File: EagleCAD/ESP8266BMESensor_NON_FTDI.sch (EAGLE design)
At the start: 21 parts, among them J1 AMP FCI 10103594-0001LF

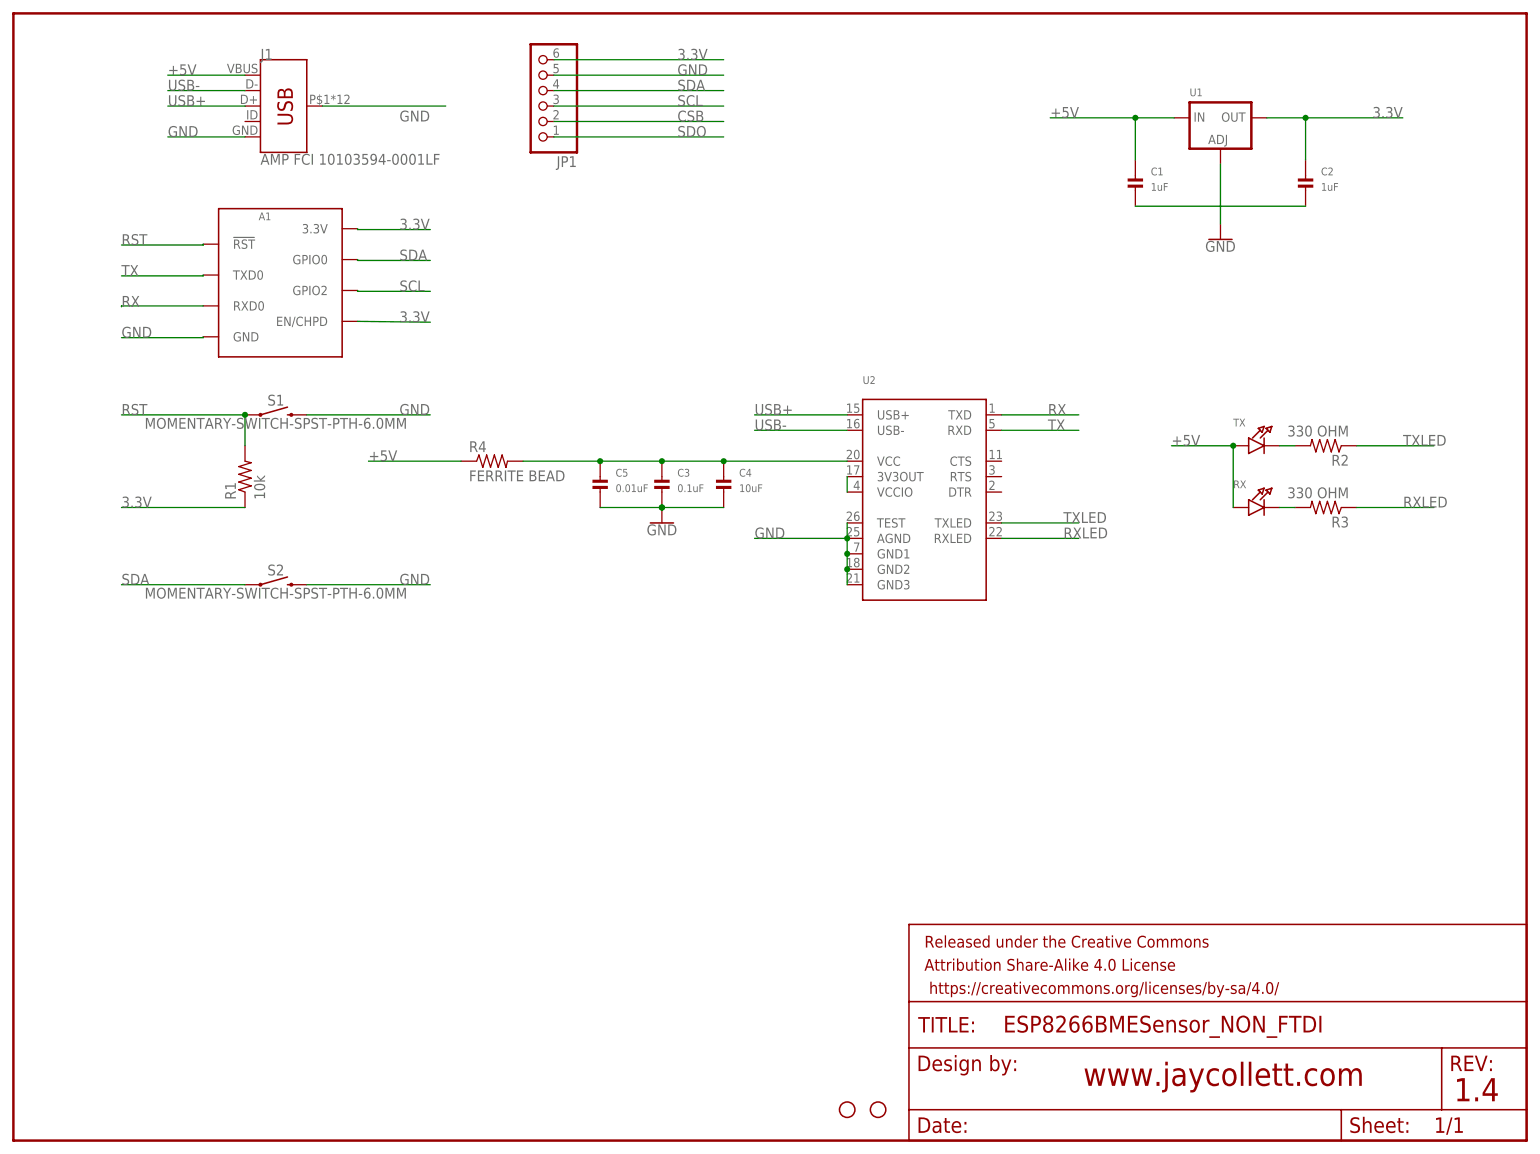
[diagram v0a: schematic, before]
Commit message: adding back the FTDI version as the primary
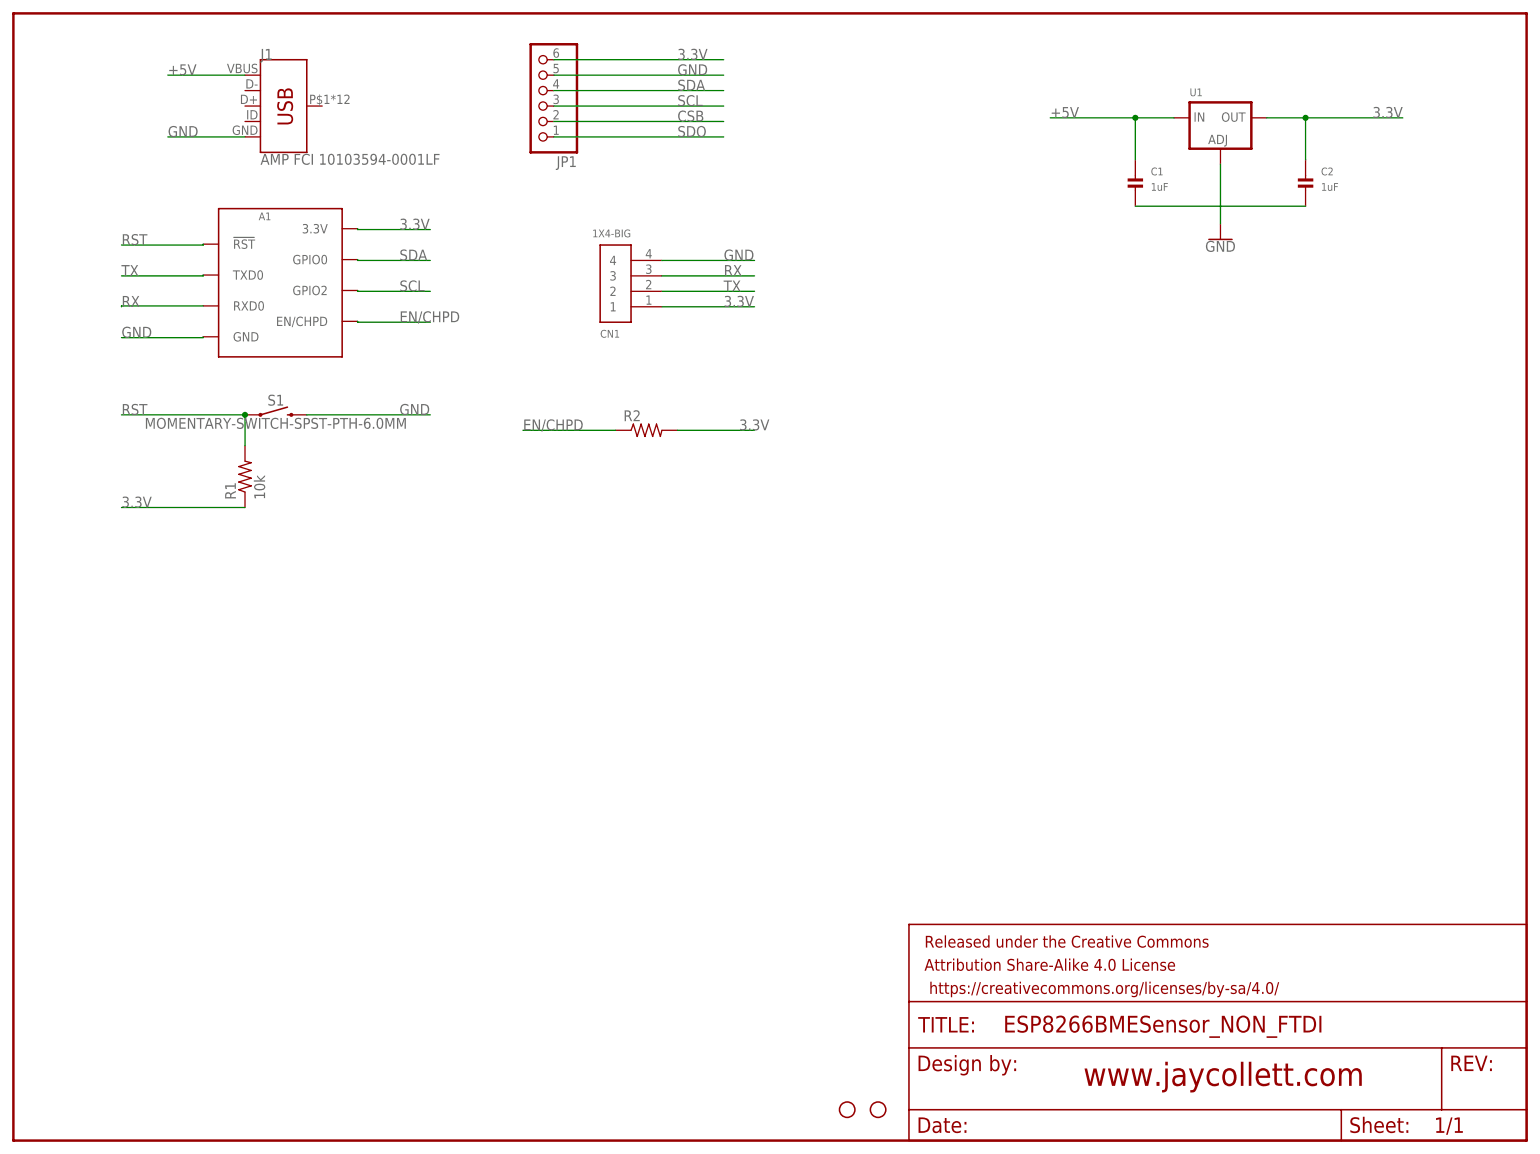
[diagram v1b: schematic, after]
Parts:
- removed C3: 0.1uF, microbuilder:CAP_CERAMIC0805
- removed C4: 10uF, microbuilder:CAP_CERAMIC0805
- removed C5: 0.01uF, microbuilder:CAP_CERAMIC0805
- removed R3: 330 OHM, adafruit:R-US_R0805
- removed R4: FERRITE BEAD, adafruit:R-US_M0805
- removed RX, TX: (no value), microbuilder:LED0805_NOOUTLINE
- removed S2: MOMENTARY-SWITCH-SPST-PTH-6.0MM, SparkFun-Switches:MOMENTARY-SWITCH-SPST-PTH-6.0MM
- removed U2: (no value), microbuilder:FT232RLSSOP28
- added CN1: 1X4-BIG, adafruit:1X4-BIG
- R2: value 330 OHM -> (none)
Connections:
- removed net N$2: R2.2, TX.C
- removed net N$3: R3.2, RX.C
- removed net RXLED: R3.1, U2.RXLED
- removed net TXLED: R2.1, U2.TXLED
- removed net USB+: J1.D+, U2.USB+
- removed net USB-: J1.D-, U2.USB-
- removed net VCCIO: U2.3V3OUT, U2.VCCIO
- new net EN/CHPD: A1.EN/CHPD, R2.1
- net +5V: no longer C3.P$1, C4.P$1, C5.P$1, R4.1, R4.2, RX.A, TX.A, U2.VCC
- net 3.3V: now also CN1.1, R2.2; no longer A1.EN/CHPD
- net GND: now also CN1.4; no longer C3.P$2, C4.P$2, C5.P$2, J1.SHIELD, S2.2, U2.AGND, U2.GND1, U2.GND2, U2.GND3, U2.TEST
- net RX: now also CN1.3; no longer U2.TXD
- net SDA: no longer S2.1
- net TX: now also CN1.2; no longer U2.RXD
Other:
- note removed: "1.4"
- moved on the sheet: R2
